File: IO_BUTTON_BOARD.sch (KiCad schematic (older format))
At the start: 113 parts, among them P1 I2C, P10 IO_7, P2 I2C, P3 IO_0, P4 IO_1, P5 IO_2, P6 IO_3, P7 IO_4, P8 IO_5, P9 IO_6, Q1 NPN, Q10 PNP, Q11 PNP, Q12 PNP, Q13 PNP, Q2 PNP, Q3 NPN, Q4 PNP, Q5 NPN, Q6 PNP, Q7 PNP, Q8 PNP, Q9 PNP, SW1 I2C_ADDR, SW2 SW_0, SW3 SW_1, SW4 SW_2, SW5 SW_3, SW6 SW_4, SW7 SW_5, SW8 SW_6, SW9 SW_7, U1 PCF8574A, U2 74HC86, U3 74HC86

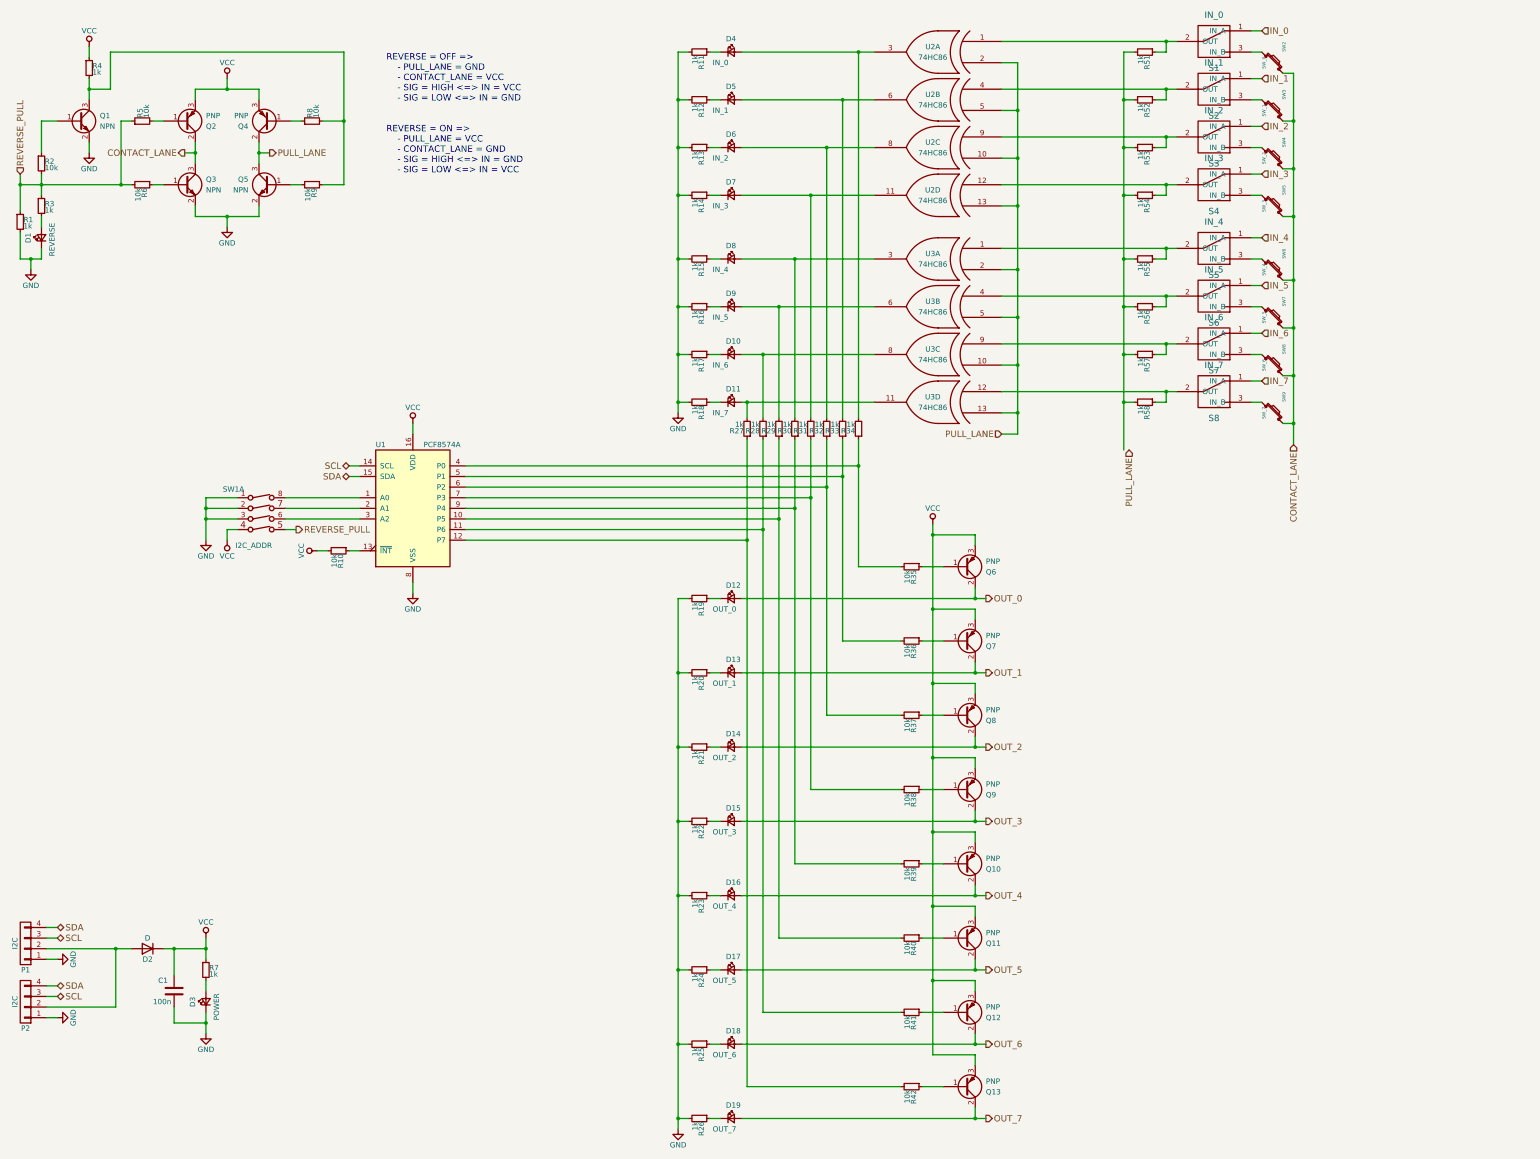
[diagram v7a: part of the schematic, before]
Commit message: Add switch to switch between Input and Ouput mode
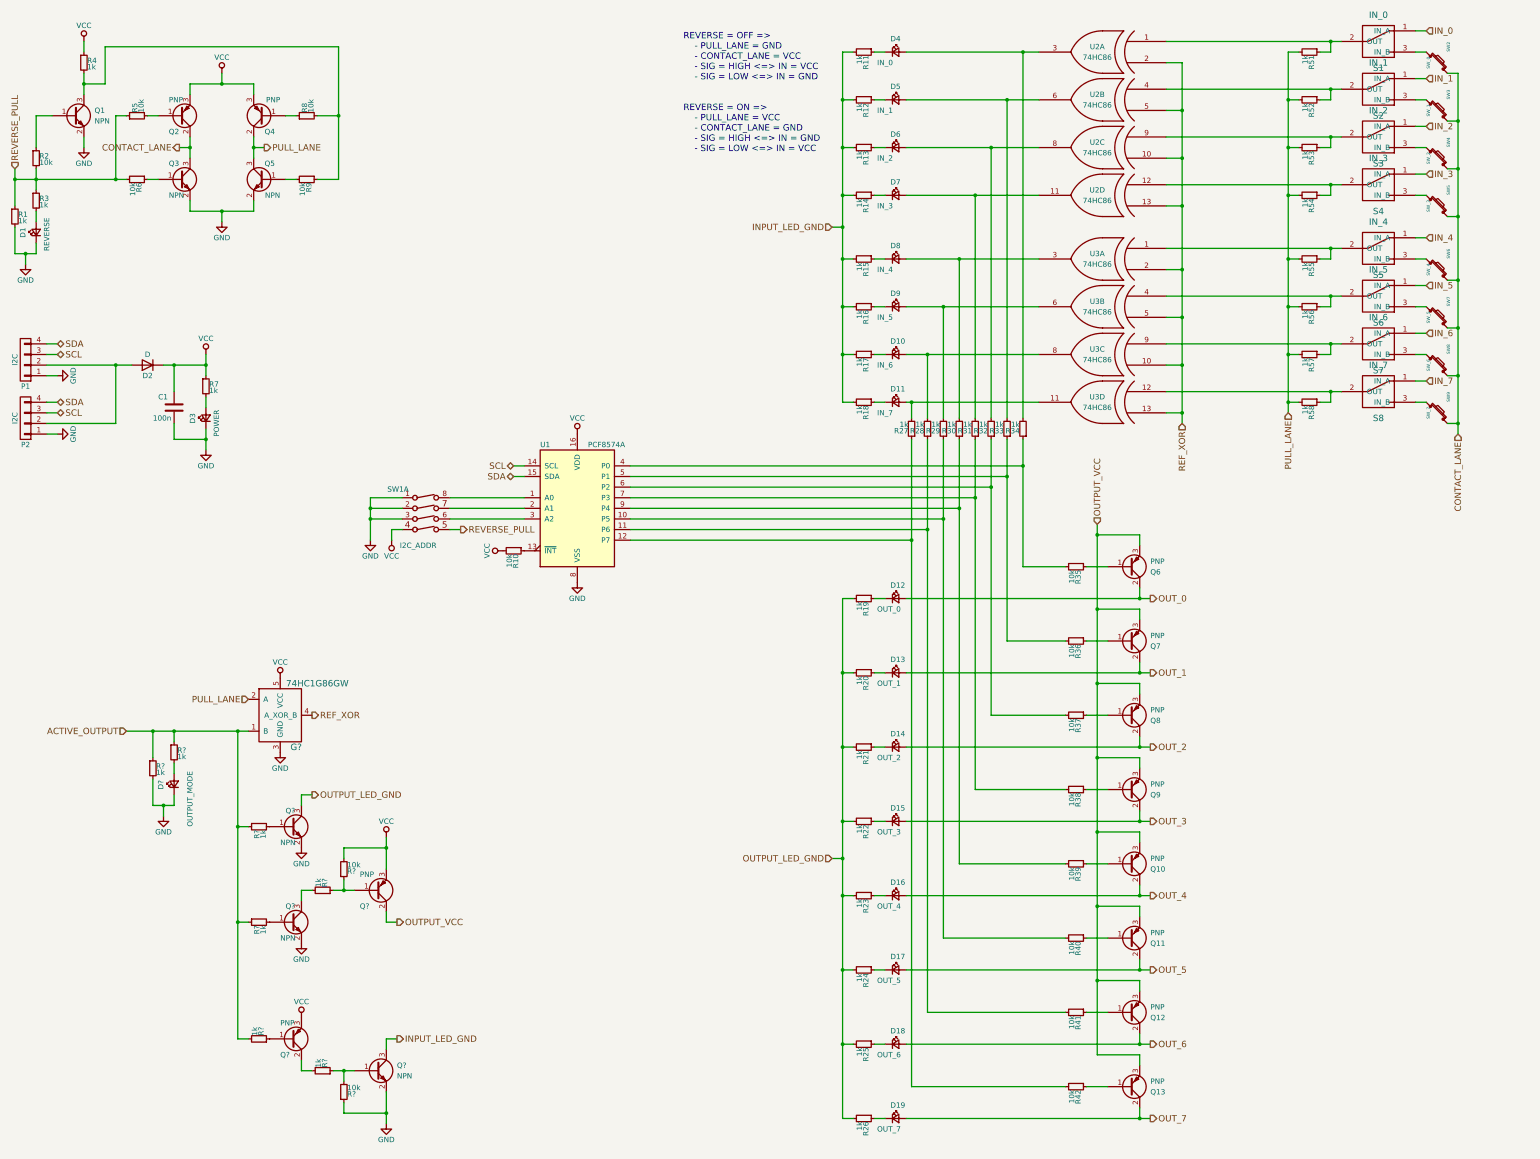
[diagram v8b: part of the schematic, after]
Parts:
- added D?: OUTPUT_MODE, LEDs:LED_0805, symbol LED_Small
- added G?: 74HC1G86GW, symbol 74HC1G86GW
- added Q?: PNP, symbol Q_PNP_BCE
- added Q? (x3): NPN, TO_SOT_Packages_SMD:SOT-23, symbol Q_NPN_BEC
- added Q?: PNP, TO_SOT_Packages_SMD:SOT-23, symbol Q_PNP_BCE
- added R? (x5): 1k, symbol R_Small
- added R? (x2): 1k, Resistors_SMD:R_0805, symbol R_Small
- added R? (x2): 10k, symbol R_Small
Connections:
- net GND: now also D?.1 (K), G?.3 (GND), Q?.2 (E), Q?.2 (E), Q?.2 (E), R?.1, R?.2; no longer R11.2, R12.2, R13.2, R14.2, R15.2, R16.2, R17.2, R18.2, R19.2, R20.2, R21.2, R22.2, R23.2, R24.2, R25.2, R26.2
- net PULL_LANE: now also R51.2, R52.2, R53.2, R54.2, R55.2, R56.2, R57.2, R58.2, G?.2 (A); no longer U2.10 (IN2), U2.13 (IN2), U2.2 (IN2), U2.5 (IN2), U3.10 (IN2), U3.13 (IN2), U3.2 (IN2), U3.5 (IN2)
- net VCC: now also G?.5 (VCC), Q?.3 (E), Q?.3 (E), R?.2; no longer Q10.3 (E), Q11.3 (E), Q12.3 (E), Q13.3 (E), Q6.3 (E), Q7.3 (E), Q8.3 (E), Q9.3 (E)
- new net: Q?.1 (B), R?.1, R?.1
- new net: Q?.3 (C), R?.2
- new net: Q?.1 (B), R?.1, R?.2
- new net: Q?.1 (B), R?.1
- new net: D?.2 (A), R?.2
- new net: Q?.1 (B), R?.2 (x2)
- new net: Q?.2 (C), R?.2
- new net ACTIVE_OUTPUT: G?.1 (B), R?.1, R?.1, R?.1, R?.1, R?.2
- new net INPUT_LED_GND: Q?.3 (C), R11.2, R12.2, R13.2, R14.2, R15.2, R16.2, R17.2, R18.2
- new net OUTPUT_LED_GND: Q?.3 (C), R19.2, R20.2, R21.2, R22.2, R23.2, R24.2, R25.2, R26.2
- new net OUTPUT_VCC: Q10.3 (E), Q11.3 (E), Q12.3 (E), Q13.3 (E), Q6.3 (E), Q7.3 (E), Q8.3 (E), Q9.3 (E), Q?.2 (C)
- new net REF_XOR: G?.4 (A_XOR_B), U2.10 (IN2), U2.13 (IN2), U2.2 (IN2), U2.5 (IN2), U3.10 (IN2), U3.13 (IN2), U3.2 (IN2), U3.5 (IN2)
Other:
- moved on the sheet: C1, D1, D10, D11, D12, D13, D14, D15, D16, D17, D18, D19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
